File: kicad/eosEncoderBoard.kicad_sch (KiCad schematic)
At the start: 72 parts, among them J1 USB_C_Receptacle_USB2.0_16P, J2 DEBUG, J3 EXTRA, SW1 RotaryEncoder, SW10 SHUTTER, SW11 SW_Push, SW2 RotaryEncoder, SW3 RotaryEncoder, SW4 RotaryEncoder, SW5 INTENS, SW6 FORM, SW7 FOCUS, SW8 IMAGE, SW9 COLOR, U1 STM32L072CZT6TR, U2 PCA9548ADB, U3 TPS62A01DRLR, Y1 OSC16M-3.3I/S3T

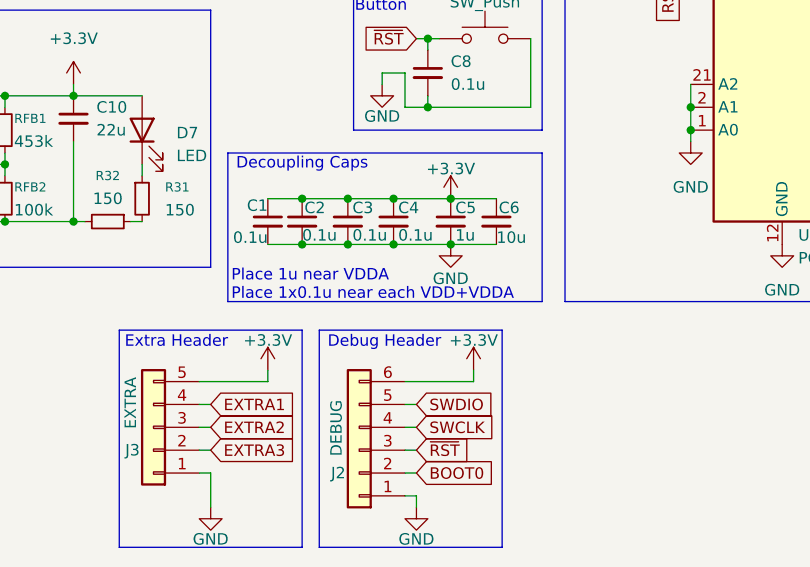
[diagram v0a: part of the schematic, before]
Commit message: some minor include optimizations, going to stick with adafruit display library
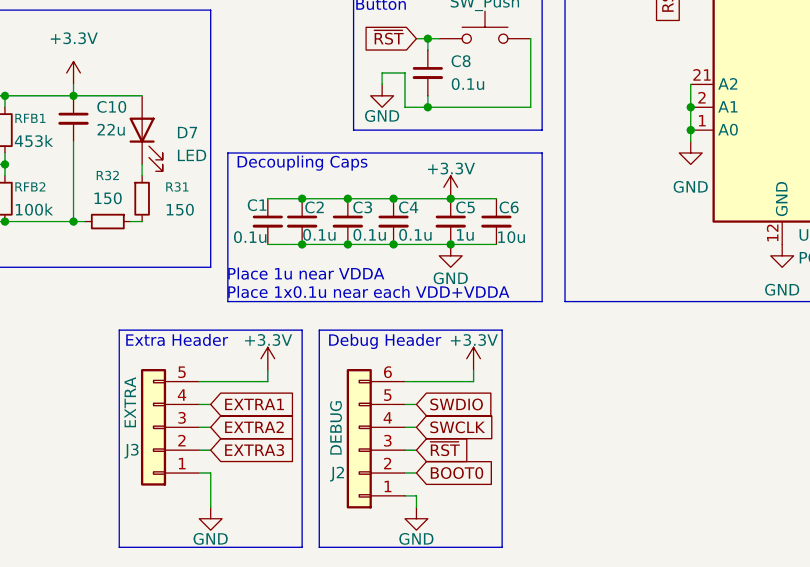
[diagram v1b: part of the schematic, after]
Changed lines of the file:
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@@
 	(text "Place 1u near VDDA\nPlace 1x0.1u near each VDD+VDDA"
 		(exclude_from_sim no)
-		(at 144.526 143.002 0)
+		(at 144.018 143.002 0)
 		(effects
 			(font

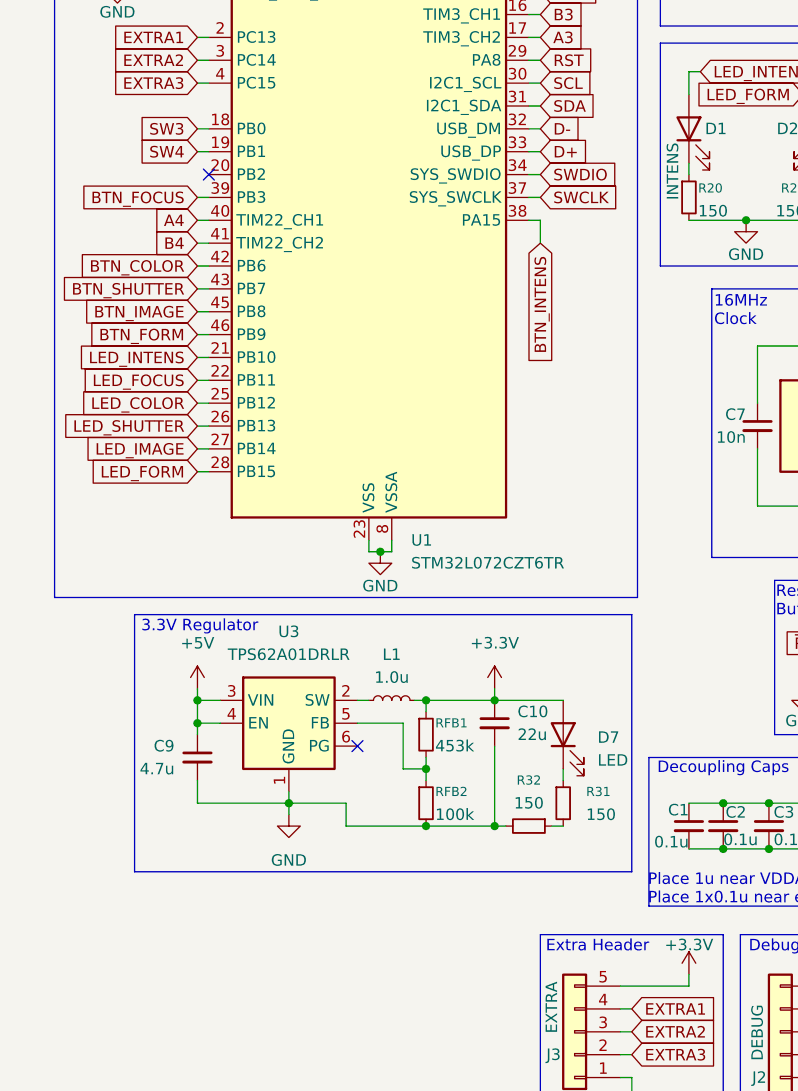
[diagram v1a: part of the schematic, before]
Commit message: move power LED to be on the MCU
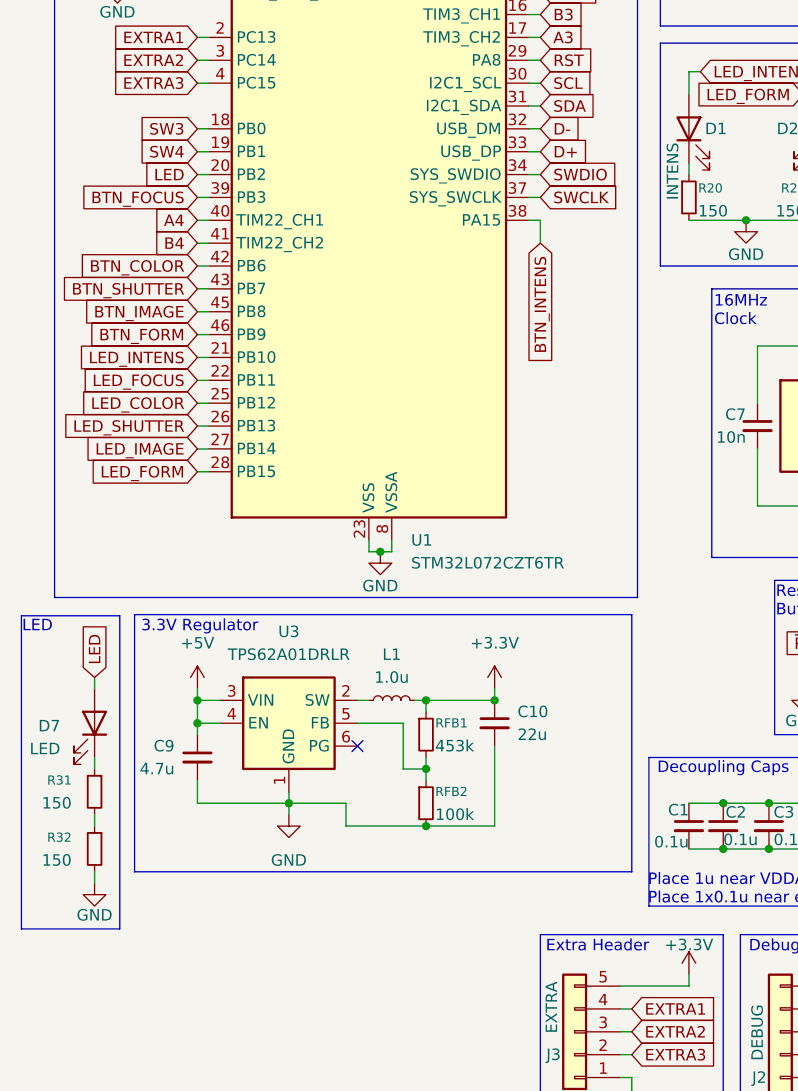
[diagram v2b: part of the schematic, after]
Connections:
- net +3.3V: no longer D7.2 (A)
- net LED: now reaches U1.20 (PB2)
- net LED: now also D7.2 (A)
- no-connect marks 18 -> 17
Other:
- note added: "LED"
